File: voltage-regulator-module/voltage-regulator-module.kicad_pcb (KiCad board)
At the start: 2 copper layers, 22.9 x 12.7 mm, 14 parts, among them J1 Power, U1 LMR16010

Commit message: Commit
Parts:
- moved R2 1.78 mm to (196.1, 122.4)
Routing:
- net GND: track 84.7 -> 108.8 mm, vias 8 -> 3
- net Net-(C3-Pad1): track 24.8 -> 18.3 mm, vias 2 -> 1
- net /Vout: track 26.9 -> 27.8 mm
- net /Vin: track 21.0 -> 20.4 mm, vias 2 -> 1
- added copper zone on B.Cu, net (none)
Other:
- board size 22.9 x 12.7 mm -> 22.9 x 13.2 mm
- net class Default: trace_width 0.254 -> 0.508; via_dia 0.762 -> 1.5; via_drill 0.396875 -> 0.5

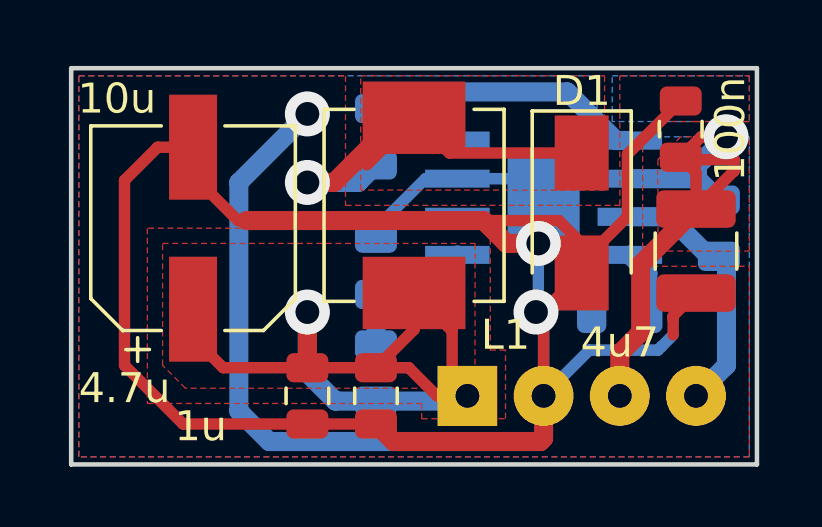
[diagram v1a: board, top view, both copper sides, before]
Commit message: PCB rev 1.1 -Fixed the TMC4671 footprint (use the Digi-Key layout) -Fixed the USB pull up issue for using the DFU bootloader -Fixed the orientation of the Hall sensor connector -Added a PTC on the hall effect sensor line -Added a 5v jumper for the CAN port
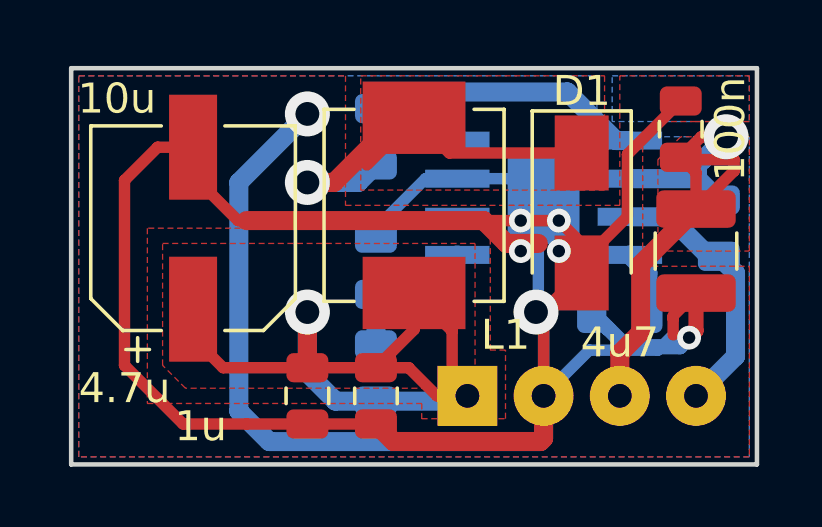
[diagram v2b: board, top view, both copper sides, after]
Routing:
- net GND: track 108.8 -> 114.3 mm, vias 3 -> 7
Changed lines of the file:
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@@
   (general
     (thickness 1.6)
-    (drawings 5)
-    (tracks 127)
+    (drawings 6)
+    (tracks 137)
     (zones 0)
     (modules 14)
@@
   )
   (setup
-    (last_trace_width 0.635)
+    (last_trace_width 0.508)
     (user_trace_width 0.508)
     (user_trace_width 0.635)
@@
     )
   )
+  (gr_poly (pts (xy 192.278 120.396) (xy 192.278 121.158) (xy 194.818 121.158) (xy 194.818 120.142) (xy 192.278 120.142)) (layer B.Mask) (width 0.15))
   (dimension 14.224 (width 0.3) (layer B.SilkS)
     (gr_text "0.5600 in" (at 193.548 106.866) (layer B.SilkS)
@@
   (segment (start 183.36 119.38) (end 181.864 117.884) (width 0.381) (layer F.Cu) (net 2))
   (segment (start 193.3725 120.142) (end 193.3725 118.7935) (width 0.381) (layer B.Cu) (net 2))
-  (via (at 193.3725 120.142) (size 1.5) (drill 0.79375) (layers F.Cu B.Cu) (net 2))
+  (via (at 194.056 119.38) (size 0.79375) (drill 0.41275) (layers F.Cu B.Cu) (net 2))
   (via (at 193.294 122.428) (size 1.5) (drill 0.79375) (layers F.Cu B.Cu) (net 2))
-  (segment (start 188.7705 116.713) (end 190.673 116.713) (width 0.381) (layer B.Cu) (net 3))
-  (segment (start 187.96 117.5235) (end 188.7705 116.713) (width 0.381) (layer B.Cu) (net 3))
-  (segment (start 187.6575 117.5235) (end 189.23 115.951) (width 0.381) (layer F.Cu) (net 3))
-  (segment (start 190.405 117.126) (end 189.23 115.951) (width 0.381) (layer F.Cu) (net 3))
-  (segment (start 194.818 117.126) (end 190.405 117.126) (width 0.381) (layer F.Cu) (net 3))
-  (segment (start 185.674 124.2845) (end 187.96 124.2845) (width 0.381) (layer F.Cu) (net 5))
-  (segment (start 189.23 123.0145) (end 187.96 124.2845) (width 0.381) (layer F.Cu) (net 5))
-  (segment (start 189.23 121.793) (end 189.23 123.0145) (width 0.381) (layer F.Cu) (net 5))
-  (segment (start 189.0545 124.2845) (end 187.96 124.2845) (width 0.381) (layer F.Cu) (net 5))
-  (segment (start 191.008 125.222) (end 189.992 125.222) (width 0.381) (layer F.Cu) (net 5))
-  (segment (start 189.992 125.222) (end 189.0545 124.2845) (width 0.381) (layer F.Cu) (net 5))
-  (segment (start 181.864 123.284) (end 181.864 122.334) (width 0.381) (layer F.Cu) (net 5))
-  (segment (start 185.674 124.2845) (end 182.8645 124.2845) (width 0.381) (layer F.Cu) (net 5))
-  (segment (start 182.8645 124.2845) (end 181.864 123.284) (width 0.381) (layer F.Cu) (net 5))
-  (segment (start 190.5 124.714) (end 191.008 125.222) (width 0.381) (layer F.Cu) (net 5))
-  (segment (start 189.23 121.793) (end 190.5 123.063) (width 0.381) (layer F.Cu) (net 5))
-  (segment (start 190.5 123.063) (end 190.5 124.714) (width 0.381) (layer F.Cu) (net 5))
-  (segment (start 190.8325 125.3975) (end 191.008 125.222) (width 0.635) (layer B.Cu) (net 5))
-  (segment (start 187.96 125.3975) (end 190.8325 125.3975) (width 0.635) (layer B.Cu) (net 5))
-  (segment (start 199.644 120.8255) (end 199.39 120.5715) (width 0.635) (layer B.Cu) (net 6))
-  (segment (start 198.628 125.222) (end 199.644 124.206) (width 0.635) (layer B.Cu) (net 6))
-  (segment (start 199.644 124.206) (end 199.644 120.8255) (width 0.635) (layer B.Cu) (net 6))
   (segment (start 195.2475 122.428) (end 195.2475 121.6985) (width 0.635) (layer B.Cu) (net 2))
   (via (at 185.674 115.824) (size 1.5) (drill 0.79375) (layers F.Cu B.Cu) (net 2))
@@
   (segment (start 183.388 118.11) (end 185.674 115.824) (width 0.635) (layer B.Cu) (net 2))
   (segment (start 183.388 125.73) (end 183.388 118.11) (width 0.635) (layer B.Cu) (net 2))
+  (via (at 192.786 119.38) (size 0.79375) (drill 0.41275) (layers F.Cu B.Cu) (net 2))
+  (via (at 192.786 120.396) (size 0.79375) (drill 0.41275) (layers F.Cu B.Cu) (net 2))
+  (via (at 194.056 120.396) (size 0.79375) (drill 0.41275) (layers F.Cu B.Cu) (net 2))
+  (via (at 198.397735 123.282419) (size 0.79375) (drill 0.41275) (layers F.Cu B.Cu) (net 2))
+  (segment (start 198.628 123.052154) (end 198.397735 123.282419) (width 0.508) (layer F.Cu) (net 2))
+  (segment (start 198.628 121.796) (end 198.628 123.052154) (width 0.508) (layer F.Cu) (net 2))
+  (segment (start 195.706737 122.984237) (end 195.1505 122.428) (width 0.508) (layer B.Cu) (net 2))
+  (segment (start 196.30771 123.58521) (end 195.706737 122.984237) (width 0.508) (layer B.Cu) (net 2))
+  (segment (start 198.094944 123.58521) (end 196.30771 123.58521) (width 0.508) (layer B.Cu) (net 2))
+  (segment (start 198.397735 123.282419) (end 198.094944 123.58521) (width 0.508) (layer B.Cu) (net 2))
+  (segment (start 188.7705 116.713) (end 190.673 116.713) (width 0.381) (layer B.Cu) (net 3))
+  (segment (start 187.96 117.5235) (end 188.7705 116.713) (width 0.381) (layer B.Cu) (net 3))
+  (segment (start 187.6575 117.5235) (end 189.23 115.951) (width 0.381) (layer F.Cu) (net 3))
+  (segment (start 190.405 117.126) (end 189.23 115.951) (width 0.381) (layer F.Cu) (net 3))
+  (segment (start 194.818 117.126) (end 190.405 117.126) (width 0.381) (layer F.Cu) (net 3))
   (via (at 185.674 118.10929) (size 1.5) (drill 0.79375) (layers F.Cu B.Cu) (net 3))
   (segment (start 186.73466 118.10929) (end 185.674 118.10929) (width 0.635) (layer B.Cu) (net 3))
@@
   (segment (start 187.96 115.6485) (end 188.516237 115.092263) (width 0.635) (layer B.Cu) (net 4))
   (segment (start 188.516237 115.092263) (end 194.340263 115.092263) (width 0.635) (layer B.Cu) (net 4))
+  (segment (start 185.674 124.2845) (end 187.96 124.2845) (width 0.381) (layer F.Cu) (net 5))
+  (segment (start 189.23 123.0145) (end 187.96 124.2845) (width 0.381) (layer F.Cu) (net 5))
+  (segment (start 189.23 121.793) (end 189.23 123.0145) (width 0.381) (layer F.Cu) (net 5))
+  (segment (start 189.0545 124.2845) (end 187.96 124.2845) (width 0.381) (layer F.Cu) (net 5))
+  (segment (start 191.008 125.222) (end 189.992 125.222) (width 0.381) (layer F.Cu) (net 5))
+  (segment (start 189.992 125.222) (end 189.0545 124.2845) (width 0.381) (layer F.Cu) (net 5))
+  (segment (start 181.864 123.284) (end 181.864 122.334) (width 0.381) (layer F.Cu) (net 5))
+  (segment (start 185.674 124.2845) (end 182.8645 124.2845) (width 0.381) (layer F.Cu) (net 5))
+  (segment (start 182.8645 124.2845) (end 181.864 123.284) (width 0.381) (layer F.Cu) (net 5))
+  (segment (start 190.5 124.714) (end 191.008 125.222) (width 0.381) (layer F.Cu) (net 5))
+  (segment (start 189.23 121.793) (end 190.5 123.063) (width 0.381) (layer F.Cu) (net 5))
+  (segment (start 190.5 123.063) (end 190.5 124.714) (width 0.381) (layer F.Cu) (net 5))
+  (segment (start 190.8325 125.3975) (end 191.008 125.222) (width 0.635) (layer B.Cu) (net 5))
+  (segment (start 187.96 125.3975) (end 190.8325 125.3975) (width 0.635) (layer B.Cu) (net 5))
   (segment (start 185.674 124.2845) (end 185.674 122.936) (width 0.635) (layer F.Cu) (net 5))
   (via (at 185.674 122.428) (size 1.5) (drill 0.79375) (layers F.Cu B.Cu) (net 5))
@@
   (segment (start 199.39 120.5715) (end 199.0575 120.5715) (width 0.635) (layer B.Cu) (net 6))
   (segment (start 199.0575 120.5715) (end 197.739 119.253) (width 0.635) (layer B.Cu) (net 6))
+  (segment (start 198.628 125.222) (end 199.946237 123.903763) (width 0.635) (layer B.Cu) (net 6))
+  (segment (start 199.946237 121.127737) (end 199.39 120.5715) (width 0.635) (layer B.Cu) (net 6))
+  (segment (start 199.946237 123.903763) (end 199.946237 121.127737) (width 0.635) (layer B.Cu) (net 6))
   (segment (start 197.0255 121.1255) (end 196.423 120.523) (width 0.635) (layer B.Cu) (net 7))
   (segment (start 197.0255 122.428) (end 197.0255 121.1255) (width 0.635) (layer B.Cu) (net 7))
